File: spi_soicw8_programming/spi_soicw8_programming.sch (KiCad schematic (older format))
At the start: 3 parts, among them P1 CONN_02X04, P2 CONN_01X06

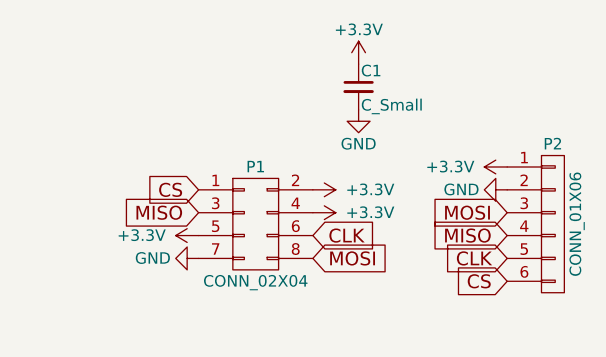
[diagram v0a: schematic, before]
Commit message: Fixed SPI flash mod board, added silkscreen helpers
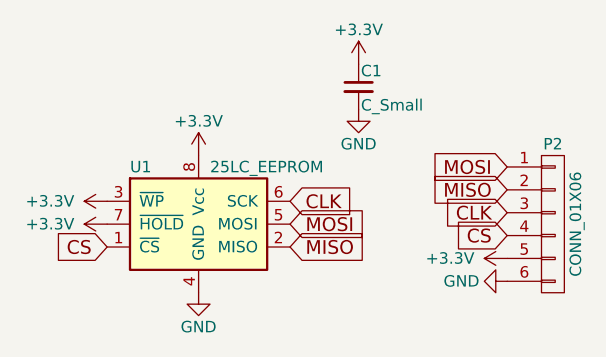
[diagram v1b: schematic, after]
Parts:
- removed P1: CONN_02X04, Housings_SOIC:SOIJ-8_5.3x5.3mm_Pitch1.27mm, symbol CONN_02X04
- added U1: 25LC_EEPROM, Housings_SOIC:SOIJ-8_5.3x5.3mm_Pitch1.27mm, symbol 25LC_EEPROM
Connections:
- net +3V3: now also P2.5 (P5), U1.3 (~WP), U1.7 (~HOLD), U1.8 (Vcc); no longer P2.1 (P1)
- net CLK: now also P2.3 (P3), U1.6 (SCK); no longer P2.5 (P5)
- net CS: now also P2.4 (P4), U1.1 (~CS); no longer P2.6 (P6)
- net GND: now also P2.6 (P6), U1.4 (GND); no longer P2.2 (P2)
- net MISO: now also P2.2 (P2), U1.2 (MISO); no longer P2.4 (P4)
- net MOSI: now also P2.1 (P1), U1.5 (MOSI); no longer P2.3 (P3)
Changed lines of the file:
@@
-$EndComp
-$Comp
-L CONN_02X04 P1
-U 1 1 590E782D
-P 4750 3200
-F 0 "P1" H 4750 3450 50  0000 C CNN
-F 1 "CONN_02X04" H 4750 2950 50  0000 C CNN
-F 2 "Housings_SOIC:SOIJ-8_5.3x5.3mm_Pitch1.27mm" H 4750 2000 50  0001 C CNN
-F 3 "" H 4750 2000 50  0000 C CNN
-	1    4750 3200
-	1    0    0    -1
 $EndComp
 $Comp
@@
 $EndComp
 $Comp
-L +3.3V #PWR01
+L +3.3V #PWR7
 U 1 1 590E98A4
-P 5850 2950
-F 0 "#PWR01" H 5850 2800 50  0001 C CNN
-F 1 "+3.3V" V 5850 3200 50  0000 C CNN
-F 2 "" H 5850 2950 50  0000 C CNN
-F 3 "" H 5850 2950 50  0000 C CNN
-	1    5850 2950
+P 5850 3350
+F 0 "#PWR7" H 5850 3200 50  0001 C CNN
+F 1 "+3.3V" V 5850 3600 50  0000 C CNN
+F 2 "" H 5850 3350 50  0000 C CNN
+F 3 "" H 5850 3350 50  0000 C CNN
+	1    5850 3350
 	0    -1   -1   0
 $EndComp
 $Comp
-L GND #PWR02
+L GND #PWR8
 U 1 1 590E98E4
-P 5850 3050
-F 0 "#PWR02" H 5850 2800 50  0001 C CNN
-F 1 "GND" V 5850 2850 50  0000 C CNN
-F 2 "" H 5850 3050 50  0000 C CNN
-F 3 "" H 5850 3050 50  0000 C CNN
-	1    5850 3050
+P 5850 3450
+F 0 "#PWR8" H 5850 3200 50  0001 C CNN
+F 1 "GND" V 5850 3250 50  0000 C CNN
+F 2 "" H 5850 3450 50  0000 C CNN
+F 3 "" H 5850 3450 50  0000 C CNN
+	1    5850 3450
 	0    1    1    0
 $EndComp
+Text GLabel 5850 2950 0    60   Input ~ 0
+MOSI
+Text GLabel 5850 3050 0    60   Input ~ 0
+MISO
 Text GLabel 5850 3150 0    60   Input ~ 0
-MOSI
+CLK
 Text GLabel 5850 3250 0    60   Input ~ 0
-MISO
-Text GLabel 5850 3350 0    60   Input ~ 0
-CLK
-Text GLabel 5850 3450 0    60   Input ~ 0
 CS
 $Comp
-L +3.3V #PWR03
+L +3.3V #PWR5
 U 1 1 590E9977
 P 5200 2500
-F 0 "#PWR03" H 5200 2350 50  0001 C CNN
+F 0 "#PWR5" H 5200 2350 50  0001 C CNN
 F 1 "+3.3V" H 5200 2650 50  0000 C CNN
 F 2 "" H 5200 2500 50  0000 C CNN
@@
 $EndComp
 $Comp
-L GND #PWR04
+L GND #PWR6
 U 1 1 590E99A1
 P 5200 2700
-F 0 "#PWR04" H 5200 2450 50  0001 C CNN
+F 0 "#PWR6" H 5200 2450 50  0001 C CNN
 F 1 "GND" H 5200 2550 50  0000 C CNN
 F 2 "" H 5200 2700 50  0000 C CNN
@@
 	1    0    0    -1
 $EndComp
+Text GLabel 4100 3300 0    60   Input ~ 0
+CS
+Text GLabel 4900 3100 2    60   Input ~ 0
+CLK
+Text GLabel 4900 3200 2    60   Input ~ 0
+MOSI
+Text GLabel 4900 3300 2    60   Input ~ 0
+MISO
 $Comp
-L +3.3V #PWR05
-U 1 1 590E99EC
-P 5000 3050
-F 0 "#PWR05" H 5000 2900 50  0001 C CNN
-F 1 "+3.3V" V 5000 3300 50  0000 C CNN
-F 2 "" H 5000 3050 50  0000 C CNN
-F 3 "" H 5000 3050 50  0000 C CNN
-	1    5000 3050
-	0    1    1    0
+L +3.3V #PWR1
+U 1 1 590E9A54
+P 4100 3100
+F 0 "#PWR1" H 4100 2950 50  0001 C CNN
+F 1 "+3.3V" V 4100 3350 50  0000 C CNN
+F 2 "" H 4100 3100 50  0000 C CNN
+F 3 "" H 4100 3100 50  0000 C CNN
+	1    4100 3100
+	0    -1   -1   0
 $EndComp
 $Comp
-L GND #PWR06
-U 1 1 590E9A00
-P 4500 3350
-F 0 "#PWR06" H 4500 3100 50  0001 C CNN
-F 1 "GND" V 4500 3150 50  0000 C CNN
-F 2 "" H 4500 3350 50  0000 C CNN
-F 3 "" H 4500 3350 50  0000 C CNN
-	1    4500 3350
-	0    1    1    0
-$EndComp
-Text GLabel 4500 3050 0    60   Input ~ 0
-CS
-Text GLabel 5000 3250 2    60   Input ~ 0
-CLK
-Text GLabel 5000 3350 2    60   Input ~ 0
-MOSI
-Text GLabel 4500 3150 0    60   Input ~ 0
-MISO
-$Comp
-L +3.3V #PWR07
-U 1 1 590E9A40
-P 5000 3150
-F 0 "#PWR07" H 5000 3000 50  0001 C CNN
-F 1 "+3.3V" V 5000 3400 50  0000 C CNN
-F 2 "" H 5000 3150 50  0000 C CNN
-F 3 "" H 5000 3150 50  0000 C CNN
-	1    5000 3150
-	0    1    1    0
+L 25LC_EEPROM U1
+U 1 1 59A2E335
+P 4500 3200
+F 0 "U1" H 4200 3450 50  0000 L CNN
+F 1 "25LC_EEPROM" H 4550 3450 50  0000 L CNN
+F 2 "Housings_SOIC:SOIJ-8_5.3x5.3mm_Pitch1.27mm" H 4150 3150 50  0001 C CNN
+F 3 "" H 4150 3150 50  0001 C CNN
+	1    4500 3200
+	1    0    0    -1
 $EndComp
 $Comp
-L +3.3V #PWR08
-U 1 1 590E9A54
-P 4500 3250
-F 0 "#PWR08" H 4500 3100 50  0001 C CNN
-F 1 "+3.3V" V 4500 3500 50  0000 C CNN
-F 2 "" H 4500 3250 50  0000 C CNN
-F 3 "" H 4500 3250 50  0000 C CNN
-	1    4500 3250
+L +3.3V #PWR2
+U 1 1 59A2E3F2
+P 4100 3200
+F 0 "#PWR2" H 4100 3050 50  0001 C CNN
+F 1 "+3.3V" V 4100 3450 50  0000 C CNN
+F 2 "" H 4100 3200 50  0000 C CNN
+F 3 "" H 4100 3200 50  0000 C CNN
+	1    4100 3200
 	0    -1   -1   0
 $EndComp
+$Comp
+L GND #PWR4
+U 1 1 59A2E40E
+P 4500 3500
+F 0 "#PWR4" H 4500 3250 50  0001 C CNN
+F 1 "GND" H 4500 3350 50  0000 C CNN
+F 2 "" H 4500 3500 50  0000 C CNN
+F 3 "" H 4500 3500 50  0000 C CNN
+	1    4500 3500
+	1    0    0    -1
+$EndComp
+$Comp
+L +3.3V #PWR3
+U 1 1 59A2E422
+P 4500 2900
+F 0 "#PWR3" H 4500 2750 50  0001 C CNN
+F 1 "+3.3V" H 4500 3050 50  0000 C CNN
+F 2 "" H 4500 2900 50  0000 C CNN
+F 3 "" H 4500 2900 50  0000 C CNN
+	1    4500 2900
+	1    0    0    -1
+$EndComp
 $EndSCHEMATC
